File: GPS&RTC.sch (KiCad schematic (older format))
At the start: 26 parts, among them U501 DS3231M, U502 NEO-6M, U503 AT24C32, U504 AT24C32

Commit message: Revision
    * Acomodo los datos de F.Fab y B.Fab
    * Genero ibom
    * Exporto PDF e imagenes
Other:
- moved on the sheet: C505, C506
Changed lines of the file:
@@
 Comment4 ""
 $EndDescr
-Connection ~ 8650 5425
-Wire Wire Line
-	9150 5425 8650 5425
+Connection ~ 8450 5275
+Wire Wire Line
+	8950 5275 8450 5275
 $Comp
 L 00_lib_sch:GND #PWR?
 U 1 1 615F146E
-P 9150 5425
+P 8950 5275
 AR Path="/61438B2D/615F146E" Ref="#PWR?"  Part="1"
 AR Path="/61434A7C/615F146E" Ref="#PWR?"  Part="1"
 AR Path="/61410FC3/615F146E" Ref="#PWR?"  Part="1"
 AR Path="/615DBDE4/615F146E" Ref="#PWR0189"  Part="1"
-F 0 "#PWR0189" H 9150 5175 50  0001 C CNN
-F 1 "GND" H 9155 5252 50  0001 C CNN
-F 2 "" H 9150 5425 50  0001 C CNN
-F 3 "" H 9150 5425 50  0001 C CNN
-	1    9150 5425
-	1    0    0    -1
-$EndComp
-Connection ~ 8650 5125
-Wire Wire Line
-	9150 5125 8650 5125
-Wire Wire Line
-	8150 5425 8650 5425
-Wire Wire Line
-	8150 5125 8650 5125
+F 0 "#PWR0189" H 8950 5025 50  0001 C CNN
+F 1 "GND" H 8955 5102 50  0001 C CNN
+F 2 "" H 8950 5275 50  0001 C CNN
+F 3 "" H 8950 5275 50  0001 C CNN
+	1    8950 5275
+	1    0    0    -1
+$EndComp
+Connection ~ 8450 4975
+Wire Wire Line
+	8950 4975 8450 4975
+Wire Wire Line
+	7950 5275 8450 5275
+Wire Wire Line
+	7950 4975 8450 4975
 $Comp
 L 00_lib_sch:+3.3V #PWR?
 U 1 1 615F1478
-P 9150 5125
+P 8950 4975
 AR Path="/61438B2D/615F1478" Ref="#PWR?"  Part="1"
 AR Path="/61434A7C/615F1478" Ref="#PWR?"  Part="1"
 AR Path="/61410FC3/615F1478" Ref="#PWR?"  Part="1"
 AR Path="/615DBDE4/615F1478" Ref="#PWR0190"  Part="1"
-F 0 "#PWR0190" H 9150 4975 50  0001 C CNN
-F 1 "+3V3" H 9165 5298 50  0000 C CNN
-F 2 "" H 9150 5125 50  0001 C CNN
-F 3 "" H 9150 5125 50  0001 C CNN
-	1    9150 5125
+F 0 "#PWR0190" H 8950 4825 50  0001 C CNN
+F 1 "+3V3" H 8965 5148 50  0000 C CNN
+F 2 "" H 8950 4975 50  0001 C CNN
+F 3 "" H 8950 4975 50  0001 C CNN
+	1    8950 4975
 	1    0    0    -1
 $EndComp
@@
 L 00_lib_sch:CP1 C?
 U 1 1 615F147E
-P 8150 5275
+P 7950 5125
 AR Path="/61438B2D/615F147E" Ref="C?"  Part="1"
 AR Path="/61434A7C/615F147E" Ref="C?"  Part="1"
 AR Path="/61410FC3/615F147E" Ref="C?"  Part="1"
 AR Path="/615DBDE4/615F147E" Ref="C505"  Part="1"
-F 0 "C505" H 8265 5321 50  0000 L CNN
-F 1 "10u" H 8265 5230 50  0000 L CNN
-F 2 "00_lib_fp:C_0805_2012Metric_Pad1.18x1.45mm_HandSolder" H 8150 5275 50  0001 C CNN
-F 3 "~" H 8150 5275 50  0001 C CNN
-	1    8150 5275
+F 0 "C505" H 8065 5171 50  0000 L CNN
+F 1 "10u" H 8065 5080 50  0000 L CNN
+F 2 "00_lib_fp:C_0805_2012Metric_Pad1.18x1.45mm_HandSolder" H 7950 5125 50  0001 C CNN
+F 3 "~" H 7950 5125 50  0001 C CNN
+	1    7950 5125
 	1    0    0    -1
 $EndComp
@@
 L 00_lib_sch:C C?
 U 1 1 615F1484
-P 8650 5275
+P 8450 5125
 AR Path="/61438B2D/615F1484" Ref="C?"  Part="1"
 AR Path="/61434A7C/615F1484" Ref="C?"  Part="1"
 AR Path="/61410FC3/615F1484" Ref="C?"  Part="1"
 AR Path="/615DBDE4/615F1484" Ref="C506"  Part="1"
-F 0 "C506" H 8765 5321 50  0000 L CNN
-F 1 "100n" H 8765 5230 50  0000 L CNN
-F 2 "00_lib_fp:C_0805_2012Metric_Pad1.18x1.45mm_HandSolder" H 8688 5125 50  0001 C CNN
-F 3 "~" H 8650 5275 50  0001 C CNN
-	1    8650 5275
-	1    0    0    -1
-$EndComp
-Text Notes 8000 5875 0    50   ~ 0
+F 0 "C506" H 8565 5171 50  0000 L CNN
+F 1 "100n" H 8565 5080 50  0000 L CNN
+F 2 "00_lib_fp:C_0805_2012Metric_Pad1.18x1.45mm_HandSolder" H 8488 4975 50  0001 C CNN
+F 3 "~" H 8450 5125 50  0001 C CNN
+	1    8450 5125
+	1    0    0    -1
+$EndComp
+Text Notes 7800 5725 0    50   ~ 0
 Capacitores de desacople.\nColocar lo mas cercano posible \na los pines del IC en cuestion.
 $Comp
@@
 Text Notes 550  950  0    276  Italic 55
 GPS&RTC
-Wire Notes Line width 39 style solid
-	600  1000 2950 1000
 Wire Wire Line
 	9250 2650 9650 2650
@@
 Wire Wire Line
 	1300 7350 1700 7350
+Wire Notes Line width 39 style solid
+	600  1000 2525 1000
 $EndSCHEMATC

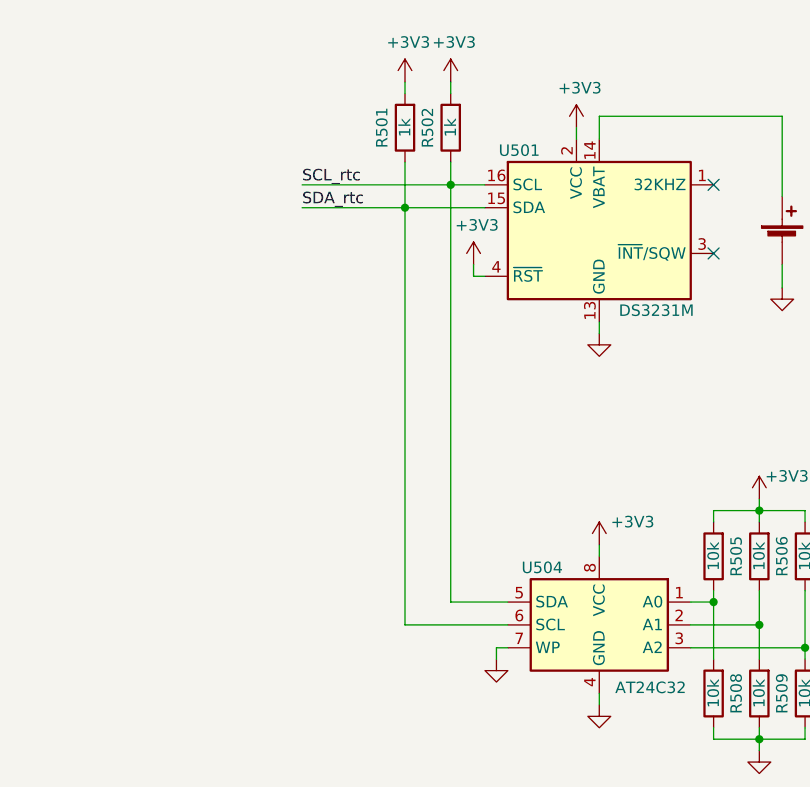
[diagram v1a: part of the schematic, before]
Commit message: Fix por revision grupal
    *Fix de memoria de i2c, mal sda y scl
    *Fix inpunts sda y scl
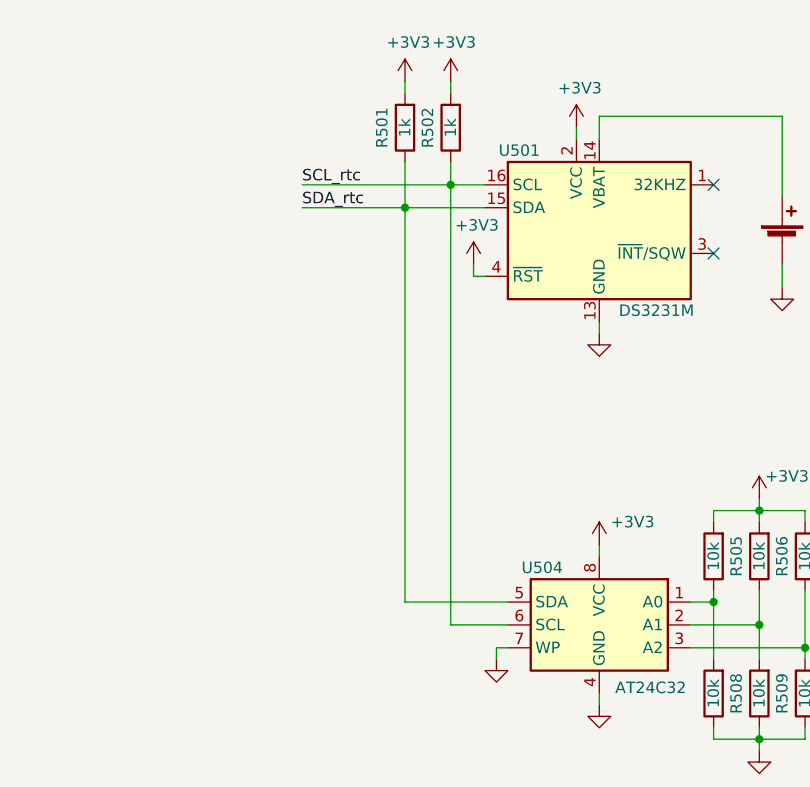
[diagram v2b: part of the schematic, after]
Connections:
- net [SCL_rtc]: now also U504.6 (SCL); no longer U504.5 (SDA)
- net [SDA_rtc]: now also U504.5 (SDA); no longer U504.6 (SCL)
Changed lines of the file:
@@
 Text HLabel 1300 7050 0    50   Input ~ 0
 [SCL_rtc]
-Connection ~ 2500 2400
-Wire Wire Line
-	2500 2400 2650 2400
-Connection ~ 2300 2500
 $Comp
 L 00_lib_sch:R R?
@@
 	-1   0    0    1
 $EndComp
-Wire Wire Line
-	2500 2400 2500 2300
 $Comp
 L 00_lib_sch:+3.3V #PWR?
@@
 Wire Wire Line
 	2300 1950 2300 2000
-Wire Wire Line
-	2300 2500 2650 2500
-Wire Wire Line
-	2300 2500 2300 2300
-Wire Wire Line
-	2300 4325 2750 4325
 $Comp
 L 00_lib_sch:+3.3V #PWR?
@@
 	3850 4475 3850 4325
 Connection ~ 3850 4325
-Wire Wire Line
-	2300 2500 2300 4325
-Wire Wire Line
-	2750 4225 2500 4225
-Wire Wire Line
-	2500 2400 2500 4225
 Connection ~ 3850 3825
 $Comp
@@
 Text Label 1850 2400 0    50   ~ 0
 SCL_rtc
-Wire Wire Line
-	1850 2400 2500 2400
 Text Label 1850 2500 0    50   ~ 0
 SDA_rtc
-Wire Wire Line
-	1850 2500 2300 2500
 Text Label 1700 7050 2    50   ~ 0
 SCL_rtc
@@
 Wire Notes Line width 39 style solid
 	600  1000 2525 1000
+Wire Wire Line
+	1850 2400 2500 2400
+Wire Wire Line
+	2650 2500 2300 2500
+Wire Wire Line
+	2300 2300 2300 2500
+Connection ~ 2300 2500
+Wire Wire Line
+	2300 2500 1850 2500
+Wire Wire Line
+	2500 2300 2500 2400
+Connection ~ 2500 2400
+Wire Wire Line
+	2500 2400 2650 2400
+Wire Wire Line
+	2300 2500 2300 4225
+Wire Wire Line
+	2300 4225 2750 4225
+Wire Wire Line
+	2500 2400 2500 4325
+Wire Wire Line
+	2500 4325 2750 4325
 $EndSCHEMATC
